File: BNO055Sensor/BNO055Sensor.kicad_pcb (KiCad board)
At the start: 4 copper layers, 50 x 35 mm, 8 parts, among them J1 locked, U1 Adafruit_BNO055_breakout

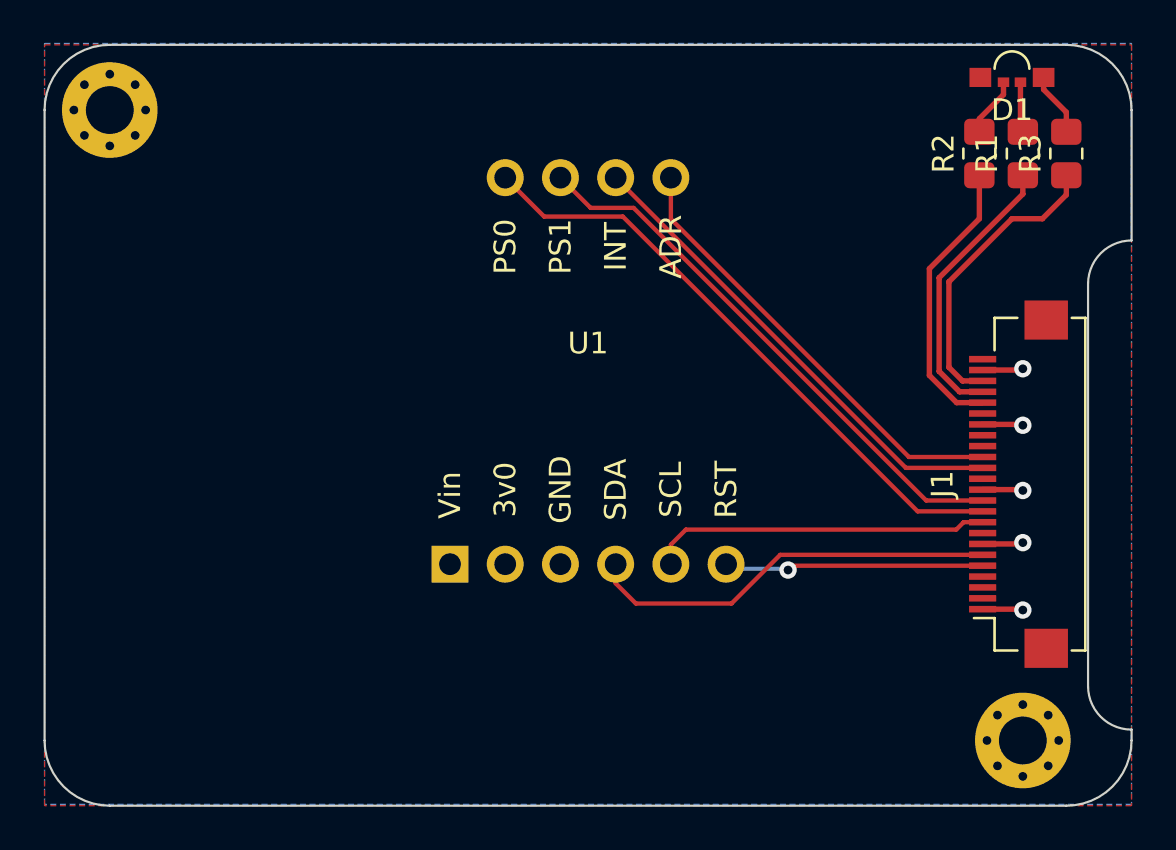
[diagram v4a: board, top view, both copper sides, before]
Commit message: Fixes DRC errors on sensor board
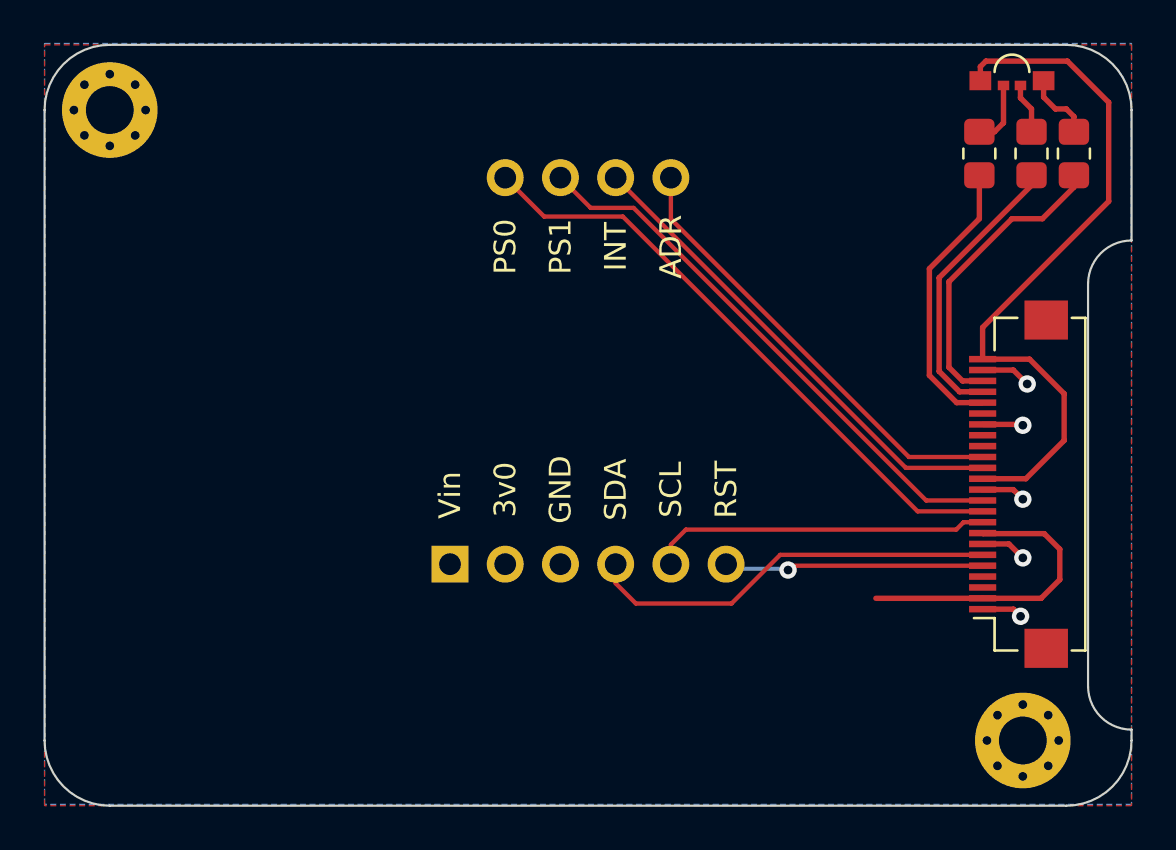
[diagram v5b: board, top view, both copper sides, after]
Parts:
- moved R1 0.40 mm to (165.4, 85.0)
- moved R3 0.35 mm to (167.3, 85.0)
- moved D1 0.15 mm to (164.5, 81.7)
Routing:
- net +3V3: track 0.00 -> 46.8 mm
- net GND: track 9.35 -> 10.2 mm

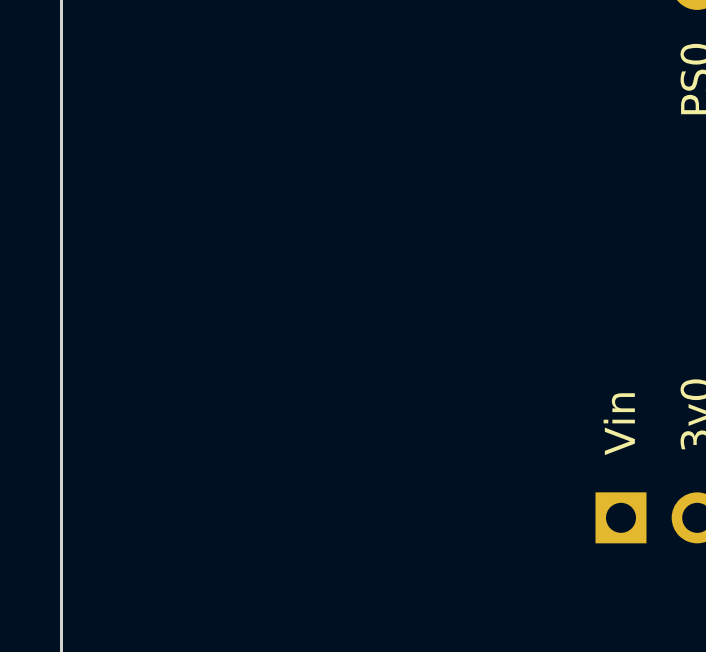
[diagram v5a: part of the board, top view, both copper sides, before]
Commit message: Adds logo and revision number to sensor board
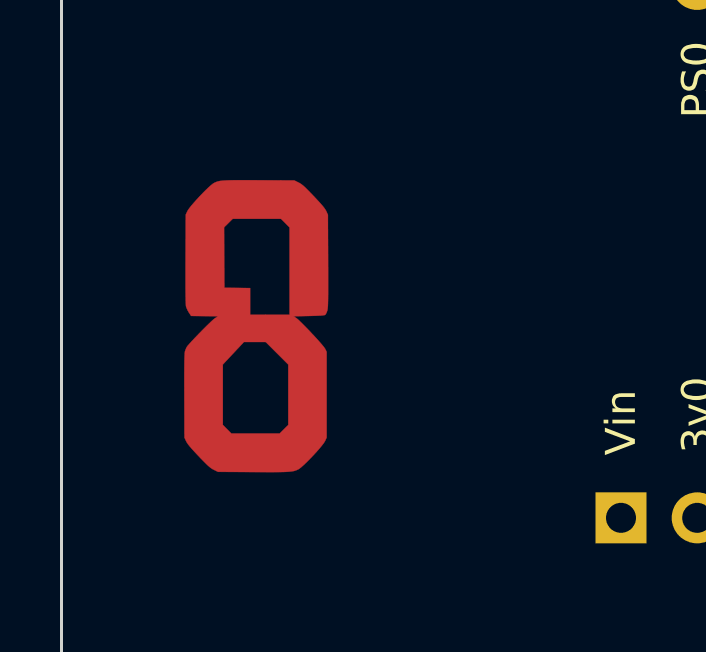
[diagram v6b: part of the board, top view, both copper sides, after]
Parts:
- added Ref**: Val**, GameOver:logo_fcu, F.Cu at (126.5, 97.5)
- added kibuzzard-6259E36C: G***, kibuzzard-6259E36C, B.Cu at (122.5, 97.5)

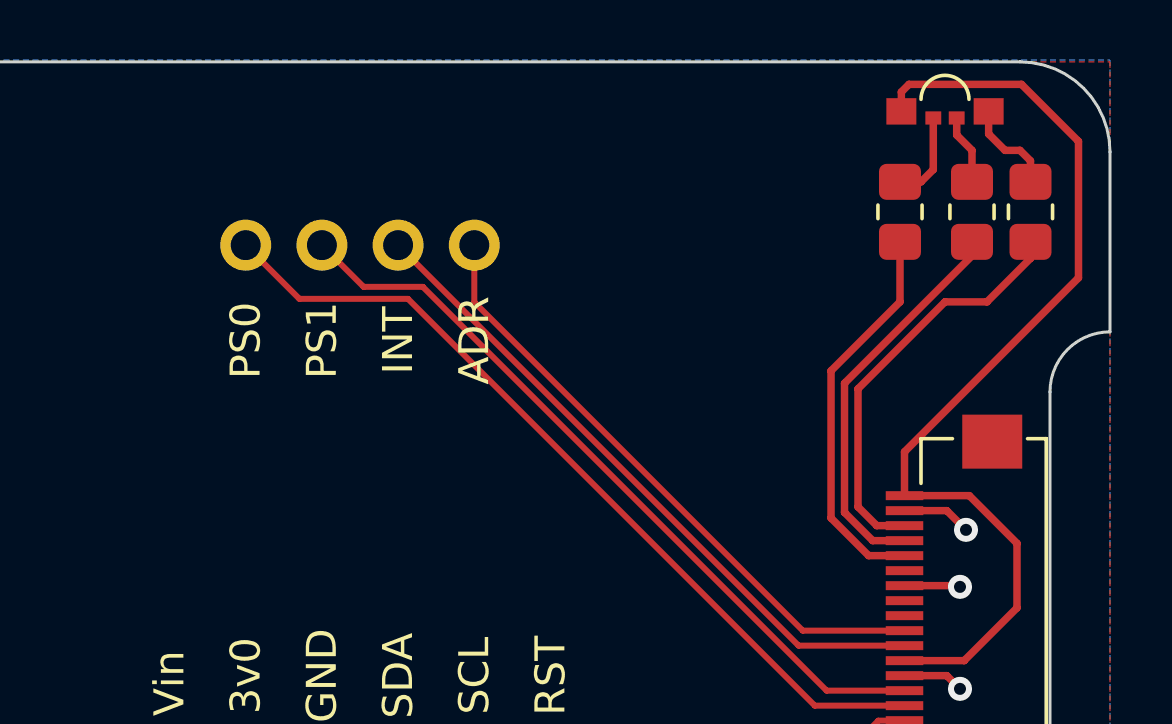
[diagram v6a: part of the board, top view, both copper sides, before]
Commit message: Adds JLCPCB order number placeholder to Sensor board
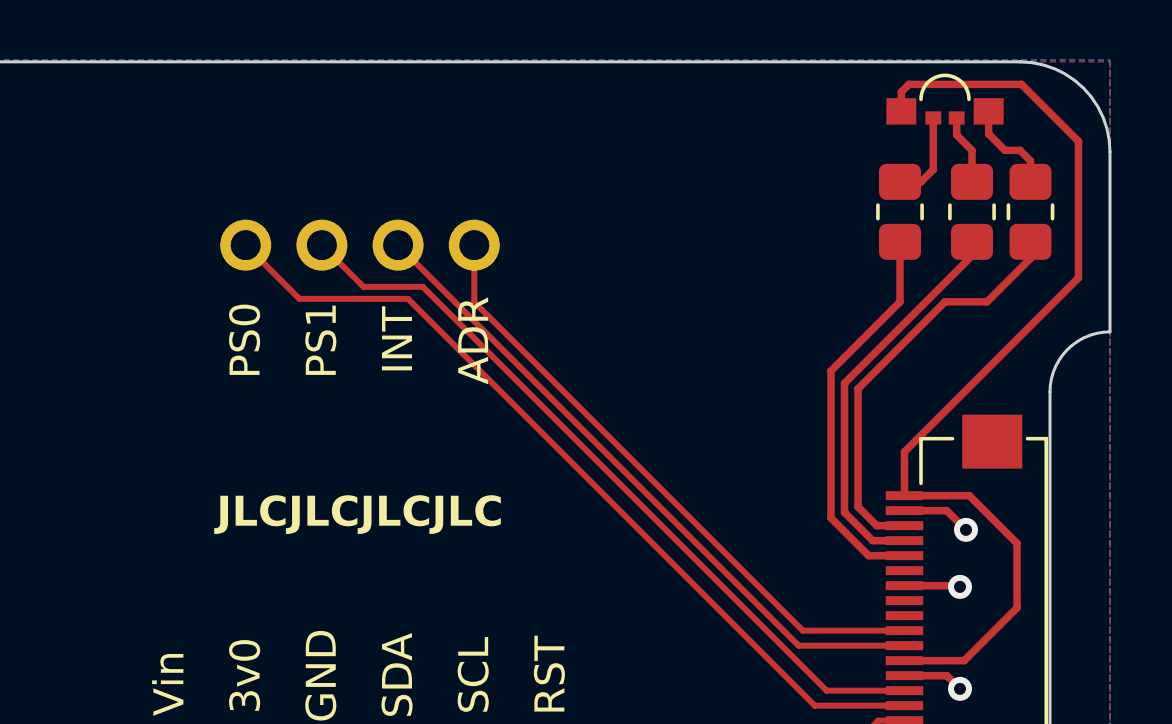
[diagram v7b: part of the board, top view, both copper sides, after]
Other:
- board text added: "JLCJLCJLCJLC"
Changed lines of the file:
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@@
       (outputformat 1)
       (mirror false)
-      (drillshape 1)
+      (drillshape 0)
       (scaleselection 1)
-      (outputdirectory "")
+      (outputdirectory "Gerber/")
     )
   )
@@
     (fp_line (start 1 0.625) (end -1 0.625)
       (stroke (width 0.1) (type solid)) (layer "F.Fab"))
-    (pad "1" smd roundrect (at -1 0 90) (size 1.2 1.4) (layers "F.Cu" "F.Paste" "F.Mask") (roundrect_rratio 0.208333)
+    (pad "1" smd roundrect (at -1 0 90) (size 1.2 1.4) (layers "F.Cu" "F.Paste" "F.Mask") (roundrect_rratio 0.2083333333)
       (net 19 "LED_G") (pintype "passive"))
-    (pad "2" smd roundrect (at 1 0 90) (size 1.2 1.4) (layers "F.Cu" "F.Paste" "F.Mask") (roundrect_rratio 0.208333)
+    (pad "2" smd roundrect (at 1 0 90) (size 1.2 1.4) (layers "F.Cu" "F.Paste" "F.Mask") (roundrect_rratio 0.2083333333)
       (net 3 "Net-(D1-GK)") (pintype "passive"))
     (model "${KICAD6_3DMODEL_DIR}/Resistor_SMD.3dshapes/R_0805_2012Metric.wrl"
@@
     (fp_line (start 1 0.625) (end -1 0.625)
       (stroke (width 0.1) (type solid)) (layer "F.Fab"))
-    (pad "1" smd roundrect (at -1 0 90) (size 1.2 1.4) (layers "F.Cu" "F.Paste" "F.Mask") (roundrect_rratio 0.208333)
+    (pad "1" smd roundrect (at -1 0 90) (size 1.2 1.4) (layers "F.Cu" "F.Paste" "F.Mask") (roundrect_rratio 0.2083333333)
       (net 20 "LED_R") (pintype "passive"))
-    (pad "2" smd roundrect (at 1 0 90) (size 1.2 1.4) (layers "F.Cu" "F.Paste" "F.Mask") (roundrect_rratio 0.208333)
+    (pad "2" smd roundrect (at 1 0 90) (size 1.2 1.4) (layers "F.Cu" "F.Paste" "F.Mask") (roundrect_rratio 0.2083333333)
       (net 2 "Net-(D1-RK)") (pintype "passive"))
     (model "${KICAD6_3DMODEL_DIR}/Resistor_SMD.3dshapes/R_0805_2012Metric.wrl"
@@
     (fp_line (start 1 0.625) (end -1 0.625)
       (stroke (width 0.1) (type solid)) (layer "F.Fab"))
-    (pad "1" smd roundrect (at -1 0 90) (size 1.2 1.4) (layers "F.Cu" "F.Paste" "F.Mask") (roundrect_rratio 0.208333)
+    (pad "1" smd roundrect (at -1 0 90) (size 1.2 1.4) (layers "F.Cu" "F.Paste" "F.Mask") (roundrect_rratio 0.2083333333)
       (net 18 "LED_B") (pintype "passive"))
-    (pad "2" smd roundrect (at 1 0 90) (size 1.2 1.4) (layers "F.Cu" "F.Paste" "F.Mask") (roundrect_rratio 0.208333)
+    (pad "2" smd roundrect (at 1 0 90) (size 1.2 1.4) (layers "F.Cu" "F.Paste" "F.Mask") (roundrect_rratio 0.2083333333)
       (net 4 "Net-(D1-BK)") (pintype "passive"))
     (model "${KICAD6_3DMODEL_DIR}/Resistor_SMD.3dshapes/R_0805_2012Metric.wrl"
@@
     (attr board_only exclude_from_pos_files exclude_from_bom)
     (fp_text reference "kibuzzard-6259E36C" (at 0 3.891492 90) (layer "B.SilkS") hide
-        (effects (font (size 0 0)) (justify mirror))
+        (effects (font (size 0 0) (thickness 0.15)) (justify mirror))
     )
     (fp_text value "G***" (at 0 -3.891492 90) (layer "B.SilkS") hide
-        (effects (font (size 0 0)) (justify mirror))
+        (effects (font (size 0 0) (thickness 0.15)) (justify mirror))
     )
     (fp_poly
@@
   (gr_arc locked (start 167 80) (mid 169.12132 80.87868) (end 170 83)
     (stroke (width 0.1) (type default)) (layer "Edge.Cuts"))
+  (gr_text "JLCJLCJLCJLC" (at 145 95) (layer "F.SilkS")
+    (effects (font (size 1 1) (thickness 0.25) bold))
+  )
   (segment (start 164.568397 105.96) (end 163.15 105.96) (width 0.25) (layer "F.Cu") (net 1))
   (segment (start 164.896184 106.287787) (end 164.568397 105.96) (width 0.25) (layer "F.Cu") (net 1))
